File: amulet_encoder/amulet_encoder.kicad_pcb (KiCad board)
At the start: 4 copper layers, 45 x 43.5 mm, 42 parts, among them J1 SM07B-GHS-TB, Q1 PMV90ENER, Q2 PMV90ENER, Q3 PMV90ENER, U1 MA732GQ, U2 SN74AHC1G02DBVR

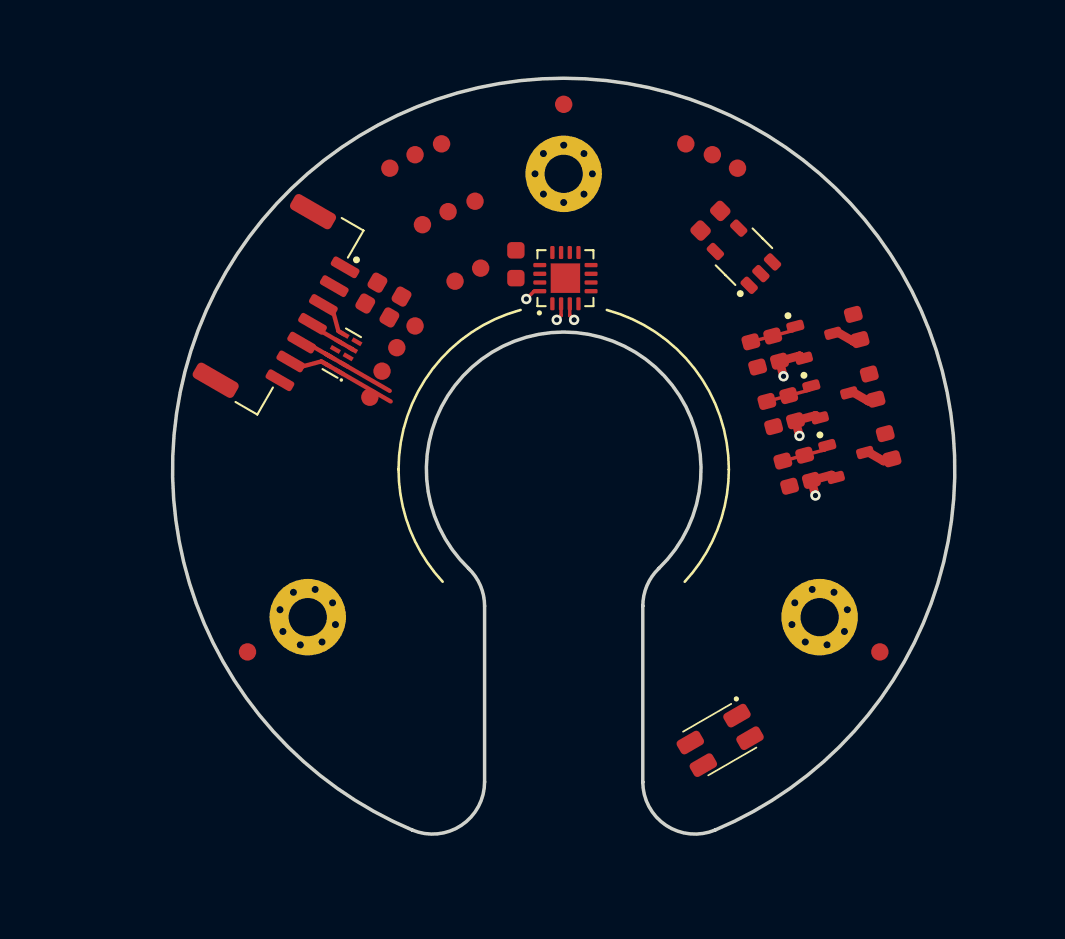
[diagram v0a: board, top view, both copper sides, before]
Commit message: preliminary layout
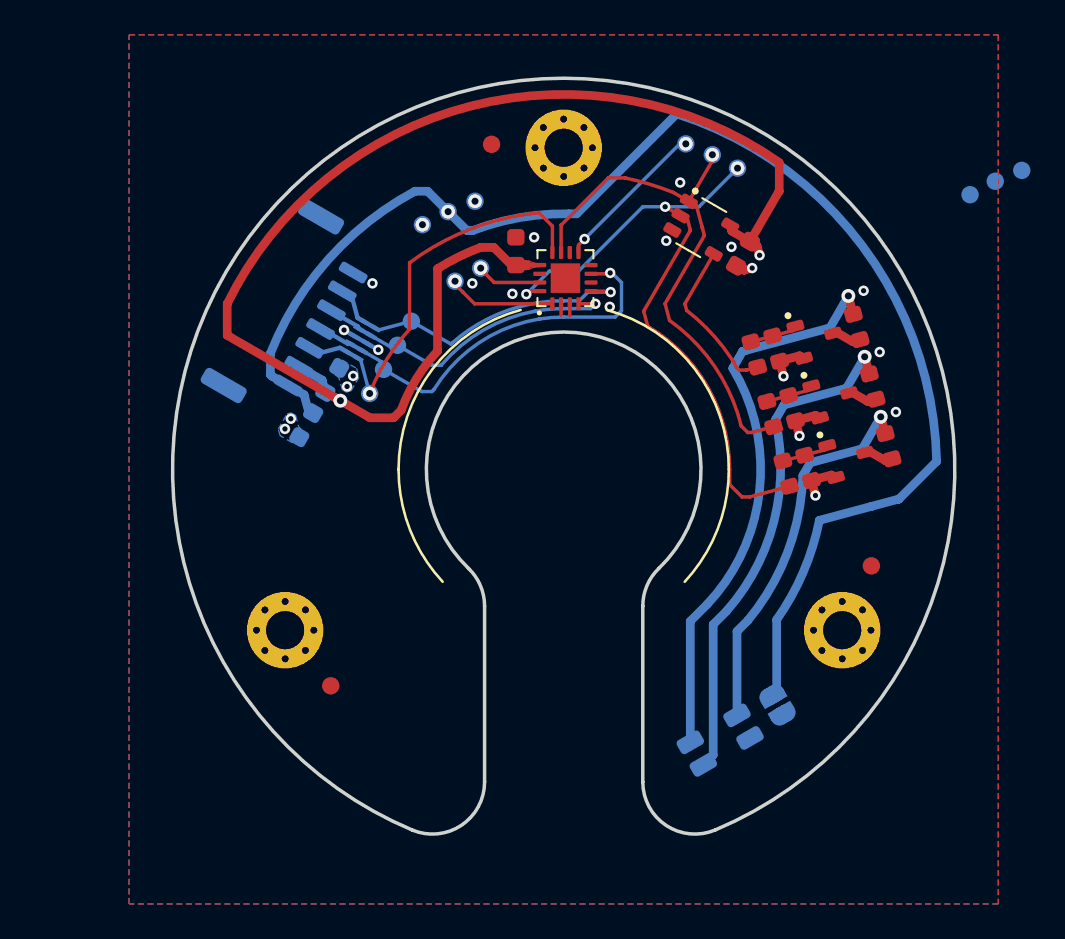
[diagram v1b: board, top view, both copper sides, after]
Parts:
- added JP1: PWR_LED, Jumper:SolderJumper-2_P1.3mm_Open_RoundedPad1.0x1.5mm, B.Cu at (160.8, 103.5)
- C1, C2, D1, D2, J1, TP1, TP10, TP11, TP12, TP13, TP14, TP15, TP2, TP3, TP4, TP5, TP6, TP7, TP8, TP9: moved to B.Cu
- moved TP7 33.4 mm to (171.9, 74.2), turned to 180 degrees
- moved TP8 33.4 mm to (173.3, 73.4), turned to 180 degrees
- moved TP9 33.4 mm to (174.8, 72.8), turned to 180 degrees
- moved C1 9.15 mm to (133.7, 87.5), turned to -120 degrees
- moved Q2 7.10 mm to (164.9, 89.3)
- moved R8 7.10 mm to (167.2, 88.7)
- moved R5 7.10 mm to (162.6, 89.9)
- moved R3 7.10 mm to (161.3, 90.2)
- moved FM1 5.17 mm to (135.1, 102.5)
- moved TP4 4.98 mm to (139.7, 81.5), turned to 180 degrees
- moved FM3 4.97 mm to (166.2, 95.5)
- moved C2 4.76 mm to (135.2, 84.9), turned to 60 degrees
- moved FM2 4.74 mm to (144.3, 71.3)
- moved TP1 4.68 mm to (137.3, 85.6), turned to 180 degrees
- moved R6 3.55 mm to (161.6, 86.5)
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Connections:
- D2 pad 4: +5V -> /LED_A
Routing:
- net +5V: track 0.00 -> 80.6 mm, vias 0 -> 1
- net +3V3: track 0.00 -> 75.6 mm, vias 0 -> 3
- net /MGH: track 1.21 -> 39.2 mm, vias 1 -> 3
- net /LED_G_K: track 0.00 -> 32.3 mm, vias 0 -> 1
- net /MGL: track 0.00 -> 30.8 mm, vias 0 -> 1
- net /LED_R_K: track 0.00 -> 28.9 mm, vias 0 -> 1
- net /CLK: track 2.24 -> 24.1 mm, vias 0 -> 1
- net /LED_Y_K: track 0.00 -> 21.8 mm, vias 0 -> 1
- net /MISO: track 2.78 -> 24.0 mm, vias 0 -> 1
- net /CS: track 6.49 -> 19.0 mm, vias 0 -> 1
- net /MOSI: track 6.19 -> 18.4 mm, vias 0 -> 1
- net /MG: track 0.00 -> 9.39 mm
- net /PWM: track 0.00 -> 9.01 mm, vias 0 -> 2
- net /SSD: track 0.00 -> 6.28 mm, vias 0 -> 1
- net /SSCK: track 0.00 -> 3.77 mm, vias 0 -> 1
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- added copper zone on F.Cu, net +3V3
- added copper zone on B.Cu, net GND
- added copper zone on F.Cu, net GND

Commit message: preliminary routing of encoder
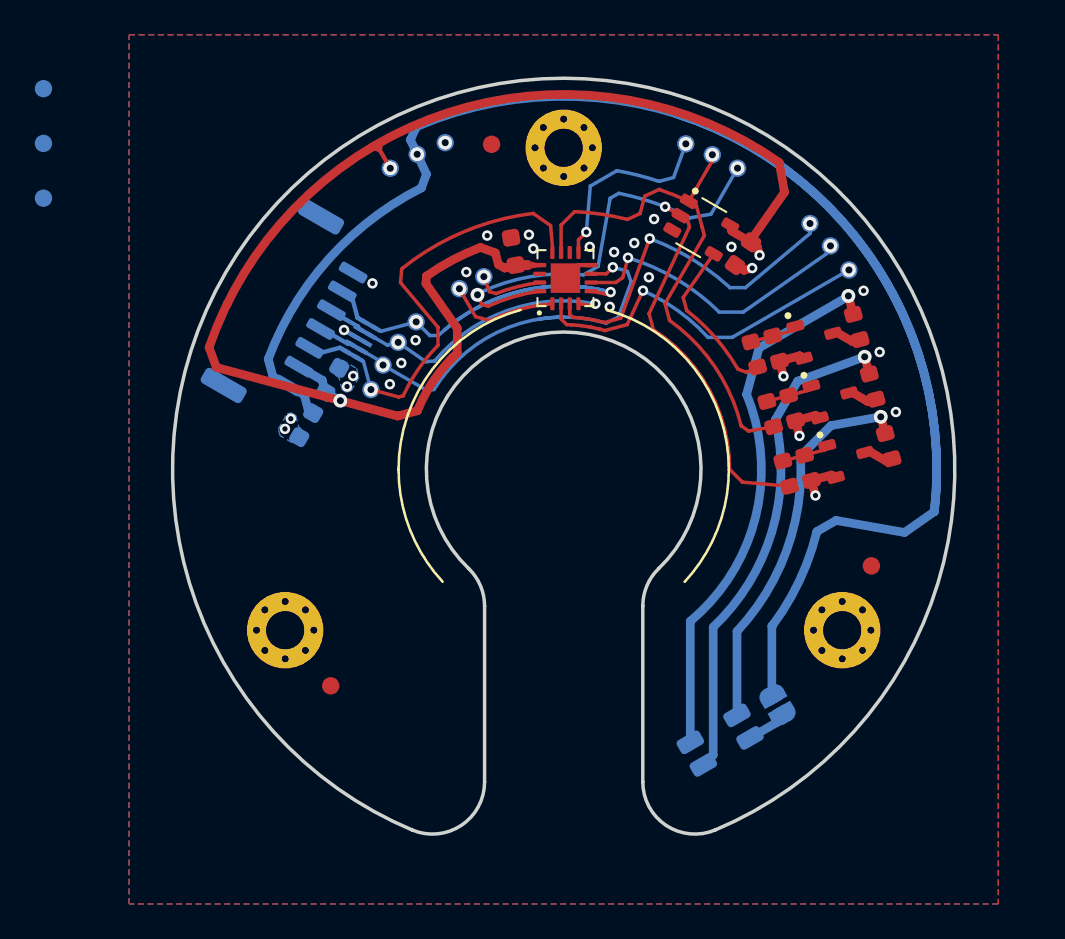
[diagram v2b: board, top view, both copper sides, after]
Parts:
- added FM4: Fiducial, 0_fiducials:Fiducial_1mm_Mask2mm, B.Cu at (118.6, 68.1)
- added FM5: Fiducial, 0_fiducials:Fiducial_1mm_Mask2mm, B.Cu at (118.6, 71.2)
- added FM6: Fiducial, 0_fiducials:Fiducial_1mm_Mask2mm, B.Cu at (118.6, 74.4)
- moved TP9 12.6 mm to (162.7, 75.9), turned to -145 degrees
- moved TP8 10.2 mm to (163.8, 77.1), turned to -135 degrees
- moved TP7 8.20 mm to (164.9, 78.5), turned to -140 degrees
- moved TP15 3.78 mm to (141.7, 71.2), turned to 110 degrees
- moved TP14 3.75 mm to (140.1, 71.9), turned to 115 degrees
- moved TP13 3.74 mm to (138.5, 72.7), turned to 120 degrees
- moved TP6 0.52 mm to (143.9, 78.9), turned to 112.5 degrees
- moved TP5 0.50 mm to (142.5, 79.6), turned to 120 degrees
- moved TP4 0.28 mm to (140.0, 81.5), turned to 90 degrees
- moved TP2 0.25 mm to (138.1, 84.0), turned to 120 degrees
- moved TP1 0.24 mm to (137.4, 85.4), turned to 136.5 degrees
- moved TP3 0.17 mm to (139.0, 82.7), turned to 106.5 degrees
- moved C4 0.14 mm to (145.6, 77.5), turned to 100 degrees
- turned C3 to -125 degrees
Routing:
- net +5V: track 80.6 -> 111.3 mm
- net /A: track 0.68 -> 20.8 mm, vias 0 -> 2
- net /Z: track 0.68 -> 20.3 mm, vias 0 -> 2
- net /B: track 0.00 -> 17.0 mm, vias 0 -> 2
- net /CS: track 19.0 -> 29.0 mm, vias 1 -> 2
- net /MGH: track 39.2 -> 46.5 mm
- net +3V3: track 75.6 -> 82.2 mm
- net /LED_A: track 0.00 -> 2.38 mm
- net /CLK: track 24.1 -> 26.4 mm
- net /MISO: track 24.0 -> 26.3 mm, vias 1 -> 2
- net /PWM: track 9.01 -> 11.3 mm
- net /LED_G_K: track 32.3 -> 30.9 mm
- net GND: track 10.4 -> 11.5 mm, vias 22 -> 28
- net /MOSI: track 18.4 -> 18.3 mm, vias 1 -> 2

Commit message: added silkscreen, better routing
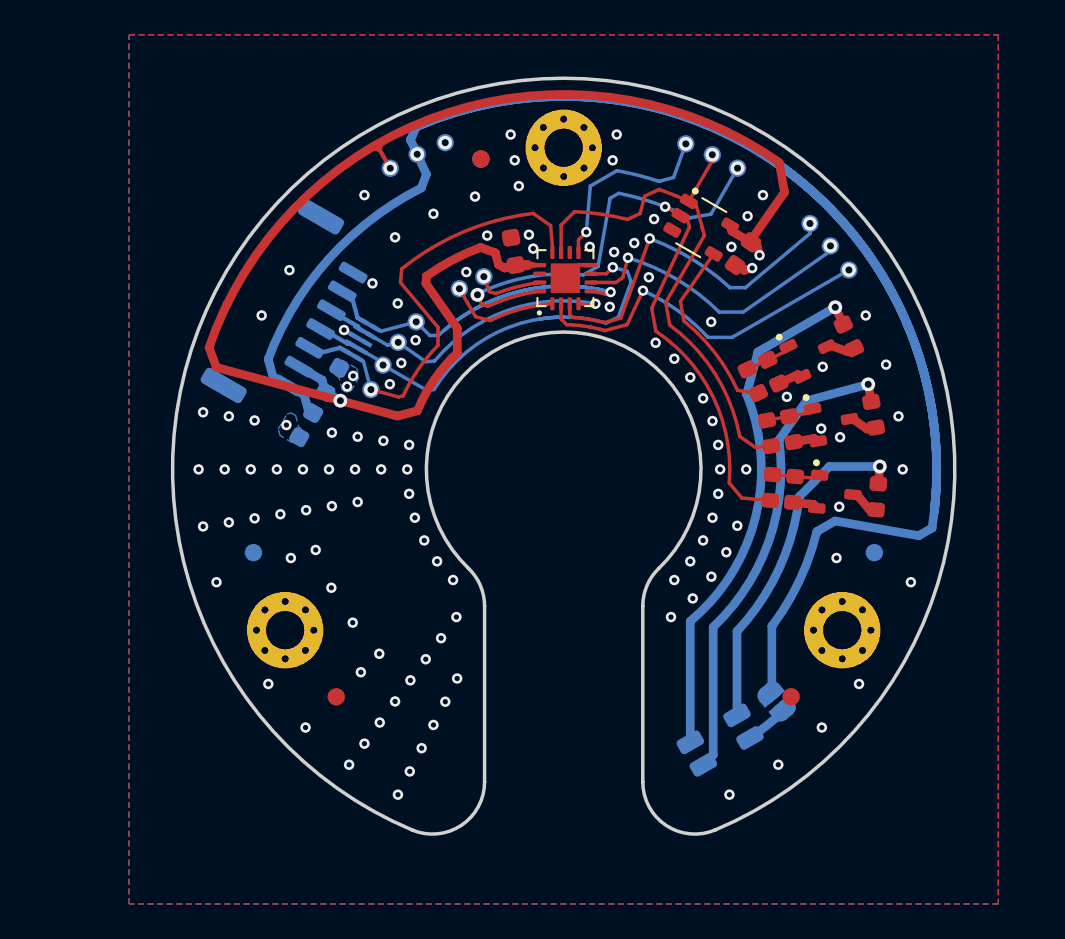
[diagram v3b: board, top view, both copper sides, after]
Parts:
- moved FM6 52.0 mm to (166.4, 94.8), turned to -60 degrees
- moved FM5 26.5 mm to (130.7, 94.8), turned to 30 degrees
- moved FM4 25.5 mm to (143.7, 72.2), turned to 90 degrees
- moved FM3 8.83 mm to (161.6, 103.1), turned to -30 degrees
- moved R8 2.98 mm to (166.5, 91.6), turned to -95 degrees
- moved Q2 2.21 mm to (164.1, 91.4), turned to -5 degrees
- moved R9 1.62 mm to (166.3, 86.9), turned to -80 degrees
- moved R1 1.54 mm to (159.4, 84.9), turned to -65 degrees
- moved R5 1.49 mm to (161.7, 91.2), turned to -95 degrees
- moved Q3 1.41 mm to (164.0, 87.3), turned to 10 degrees
- moved R2 1.34 mm to (160.6, 84.4), turned to -65 degrees
- moved R6 1.21 mm to (161.6, 87.7), turned to -80 degrees
- moved R3 1.16 mm to (160.5, 91.0), turned to -95 degrees
- moved R4 1.10 mm to (160.3, 87.9), turned to -80 degrees
- moved FM2 1.03 mm to (143.7, 72.1), turned to 150 degrees
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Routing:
- net +5V: track 111.3 -> 154.1 mm
- net GND: track 11.5 -> 8.85 mm, vias 28 -> 120
- net /LED_Y_K: track 22.2 -> 19.8 mm
- net /LED_R_K: track 28.7 -> 27.4 mm
- net /MG: track 9.57 -> 10.8 mm
- net /LED_G_K: track 30.9 -> 29.9 mm
- net /MGL: track 30.7 -> 31.3 mm
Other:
- board text added: "A"
- board text added: "C"
- board text added: "E"
- board text added: "N"
- board text added: "e"
- board text added: "l"
- board text added: "m"
- board text added: "t"
- board text added: "u"

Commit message: rough version of encoder
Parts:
- added G***: LOGO, LOGO, B.Cu at (139.0, 104.0)
- H2: value M2 -> e
- R1, R3, R4: value R -> 1k 1/10W 1%
- R2, R5, R6: value R -> 100k 1/10W 1%
- R7: value R -> 200R 1/5W 1%
- R8, R9: value R -> 330R 1/5W 1%
- TP1, TP10, TP11, TP12, TP13, TP14, TP15, TP2, TP3, TP4, TP5, TP6: footprint 0_testpoint:TestPoint_Pad_D1mm_Front -> 0_testpoint:TestPoint_Pad_D1mm_THT; moved to F.Cu
- TP7, TP8, TP9: footprint 0_testpoint:TestPoint_Pad_D1mm_Front -> 0_testpoint:TestPoint_Pad_D1mm_THT
- moved FM3 9.58 mm to (166.4, 94.8)
- moved JP1 1.58 mm to (161.9, 102.2), turned to 135 degrees
- moved D2 1.57 mm to (158.8, 104.7), turned to -55 degrees
- moved R4 1.30 mm to (161.6, 87.7)
- moved R6 1.30 mm to (160.3, 87.9)
- moved R1 1.30 mm to (160.6, 84.4)
- moved R2 1.30 mm to (159.4, 84.9)
- moved R3 1.30 mm to (161.7, 91.2)
- moved R5 1.30 mm to (160.5, 91.0)
- turned TP1 to 180 degrees
- turned TP13 to 180 degrees
- turned TP14 to 180 degrees
- turned TP15 to 180 degrees
- turned TP2 to 180 degrees
- turned TP3 to 180 degrees
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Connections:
- R2 pad 1: /MOS_G_G -> /MG
- R5 pad 1: /MOS_Y_G -> /MGH
- R6 pad 1: /MOS_R_G -> /MGL
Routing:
- net +5V: track 154.1 -> 123.7 mm, vias 1 -> 0
- net /CS: track 29.0 -> 18.9 mm, vias 2 -> 1
- net GND: track 8.85 -> 6.21 mm, vias 120 -> 112
- net /MISO: track 26.3 -> 24.7 mm, vias 2 -> 1
- net /MGH: track 46.2 -> 47.7 mm, vias 3 -> 2
- net +3V3: track 82.2 -> 80.7 mm, vias 3 -> 1
- net /LED_Y_K: track 19.8 -> 18.5 mm
- net /MOS_Y_G: track 2.78 -> 1.48 mm
- net /MOS_R_G: track 2.78 -> 1.48 mm
- net /MOS_G_G: track 2.78 -> 1.48 mm
- net /LED_G_K: track 29.9 -> 28.7 mm
- net /MGL: track 31.3 -> 32.1 mm, vias 1 -> 0
- net /MG: track 10.8 -> 11.6 mm
- net /LED_R_K: track 27.4 -> 26.7 mm
- net /MOSI: track 18.3 -> 18.1 mm, vias 2 -> 1
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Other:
- board text added: "0 16 16"
- board text added: "0 21 21"
- board text added: "0 5 5"
- board text added: "0.30mm 0.40mm 0.40mm 0.50mm 2.20mm"
- board text added: "121 5 24 15 3"
- board text added: "ASSEMBLY NOTES (UNLESS OTHERWISE SPECIFIED) 1) DO NOT POPULATE PARTS ARE MARKED WITH A RED CROSS. 2) DO NOT POPULATE PARTS ARE NOT PRESENT IN THE BOM. 3) IF CONFLICTING INFORMATION IS FOUND BETWEEN THE ASSEMBLY FILE AND BOM, BOM SHOULD BE USED AS THE MAIN SOURCE."
- board text added: "Back Side"
- board text added: "Bottom Assembly (Scale 1:1)"
- board text added: "Bottom View"
- board text added: "Components"
- board text added: "Count"
- board text added: "Drill Drawing (Top View) (Scale 1:1)"
- board text added: "Front Side"
- board text added: "Hole Size"
- board text added: "Plated"
- board text added: "Plated Plated Plated Plated Plated"
- board text added: "Symbol"
- board text added: "THT SMD Total"
- board text added: "Top Assembly (Scale 1:1)"
- board text added: "Top View"
- board text added: "Total"
- board text removed: "??mm"
- board text removed: "??mm (??oz)"
- board text removed: "B.Mask"
- board text removed: "B.Paste"
- board text removed: "B.Silkscreen"
- board text removed: "Copper"
- board text removed: "Core"
- board text removed: "Dielectric"
- board text removed: "Dielectric Material"
- board text removed: "F.Mask"
- board text removed: "F.Paste"
- board text removed: "F.Silkscreen"
- board text removed: "FABRICATION NOTES (CONT.) 3) IMPEDANCE CONTROL REQUIRED. ? Microstrip ???-Ohm Differential (L? ref. L?, L? ref. L?) ??mm width, ??mm spacing 4) CONFIRM TRACE WIDTHS AND SPACINGS. 5) DESIGN GEOMETRY MINIMUM FEATURE SIZES: TRACE WIDTH ?? mm TRACE TO TRACE ?? mm MIN. HOLE (plated) ?? mm MIN. HOLE (unplated) ?? mm ANNULAR RING ?? mm COPPER TO HOLE ?? mm COPPER TO EDGE ?? mm HOLE TO HOLE ?? mm"
- board text removed: "FABRICATION NOTES (UNLESS OTHERWISE SPECIFIED) 1) 2)"
- board text removed: "FR-4"
- board text removed: "GBR"
- board text removed: "Gerber"
- board text removed: "Internal Plane"
- board text removed: "L1 (??)"
- board text removed: "L2 (??)"
- board text removed: "L3 (??"
- board text removed: "L4 (??)"
- board text removed: "L5 (??)"
- board text removed: "L6 (??)"
- board text removed: "Layer"
- board text removed: "Layer Stack Legend"
- board text removed: "Legend"
- board text removed: "Material"
- board text removed: "Note: external layer thicknesses are specified after plating."
- board text removed: "Paste Mask"
- board text removed: "Prepreg"
- board text removed: "Signal"
- board text removed: "Solder Mask"
- board text removed: "Solder Resist"
- board text removed: "Thickness"
- board text removed: "Total thickness: 1.62mm"
